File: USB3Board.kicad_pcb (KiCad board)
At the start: 4 copper layers, 53 x 52 mm, 44 parts, among them IC1 FT600Q-B-T, U1 TPD2EUSB30, U2 TPD2EUSB30, U3 TPD2EUSB30, Y1 30Mhz

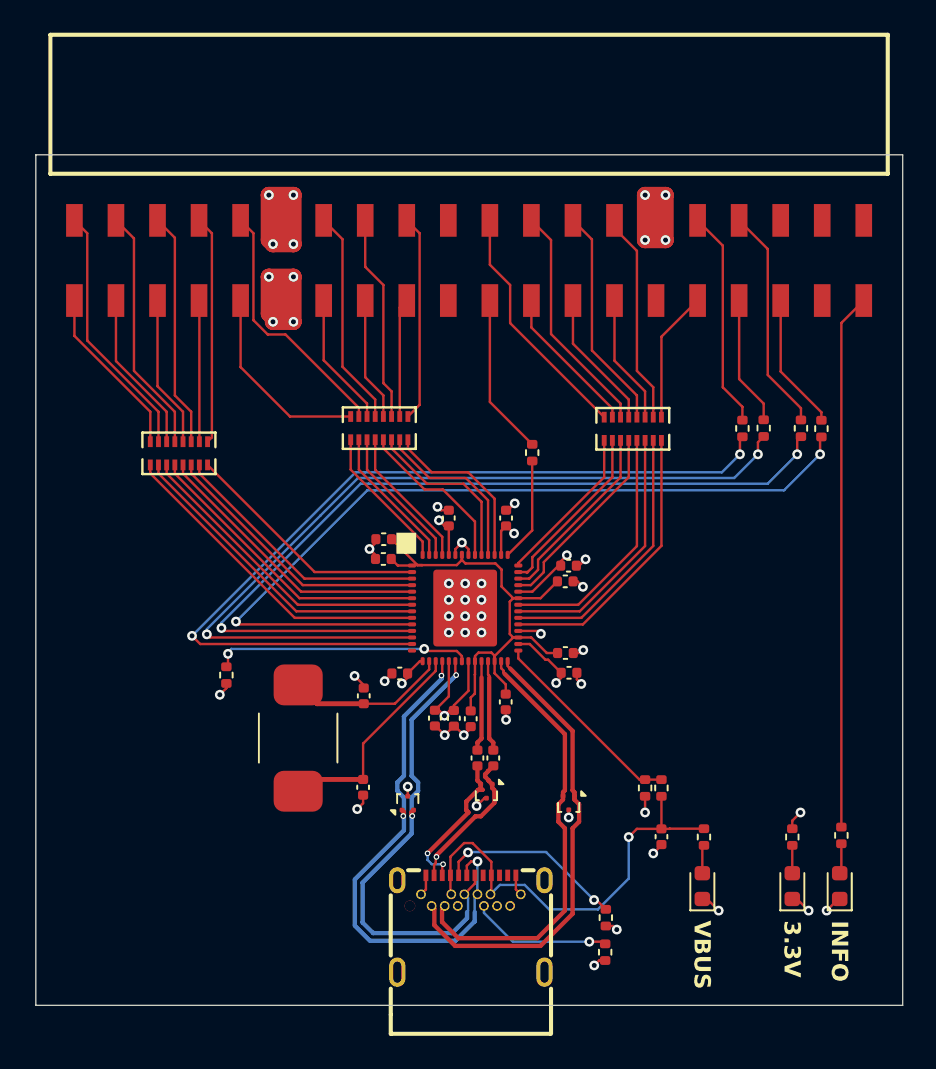
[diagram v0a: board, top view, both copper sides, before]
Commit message: Make via sizes consistent and large enough to not require special assembly Add some silkscreen to help orientation.
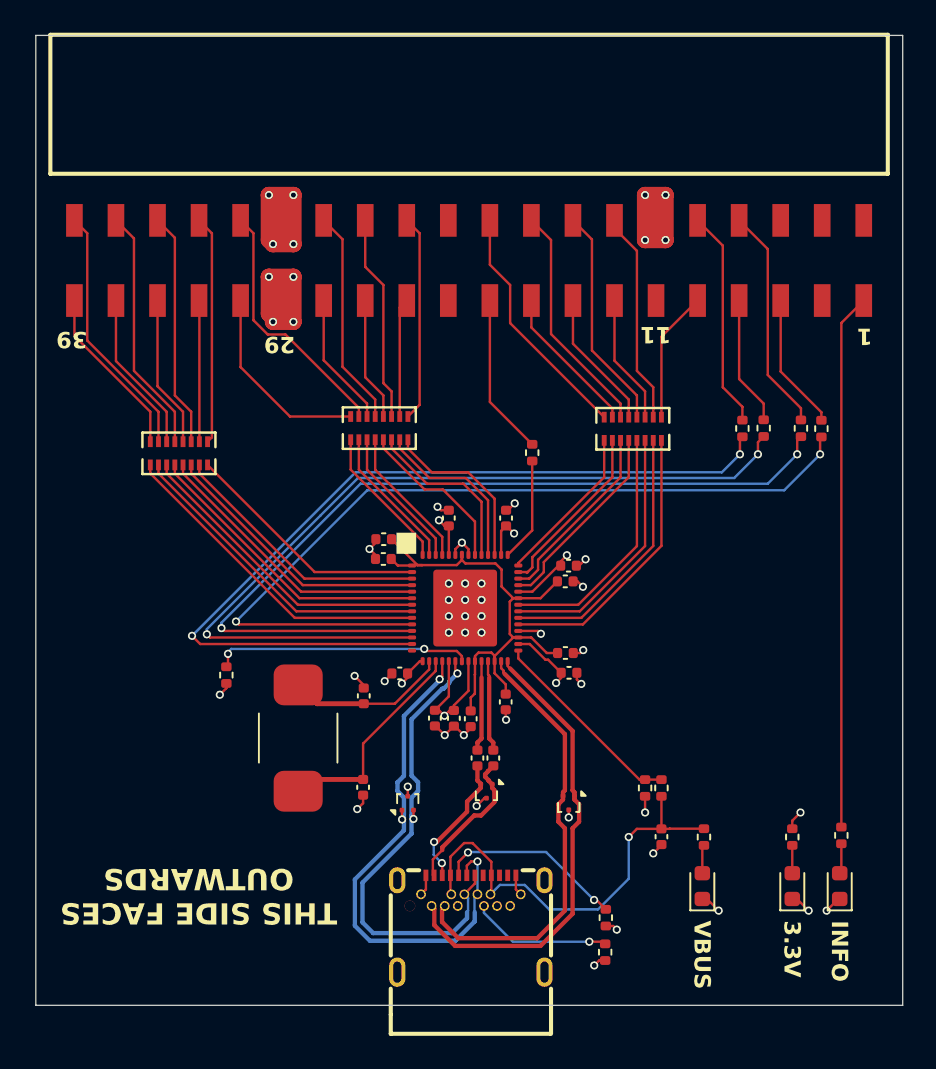
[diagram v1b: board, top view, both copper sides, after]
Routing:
- net /USB_I_TXN: track 9.49 -> 8.47 mm
- net /USB_I_TXP: track 8.85 -> 9.00 mm, vias 1 -> 0
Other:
- board size 53 x 52 mm -> 53 x 59.3 mm
- board text added: "11"
- board text added: "29"
- board text added: "39"
- board text added: "THIS SIDE FACES OUTWARDS"
